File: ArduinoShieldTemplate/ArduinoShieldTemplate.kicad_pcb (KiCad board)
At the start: 2 copper layers, 68.6 x 53.3 mm, 31 parts, among them J1 M3, J2 M3, J3 M3, J4 Barrel_Jack_Switch, J5 UC_Screw_Terminal_01X02, J6 UC_Screw_Terminal_01X02, P1 Power, P2 Analog, P3 Digital, P4 Digital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

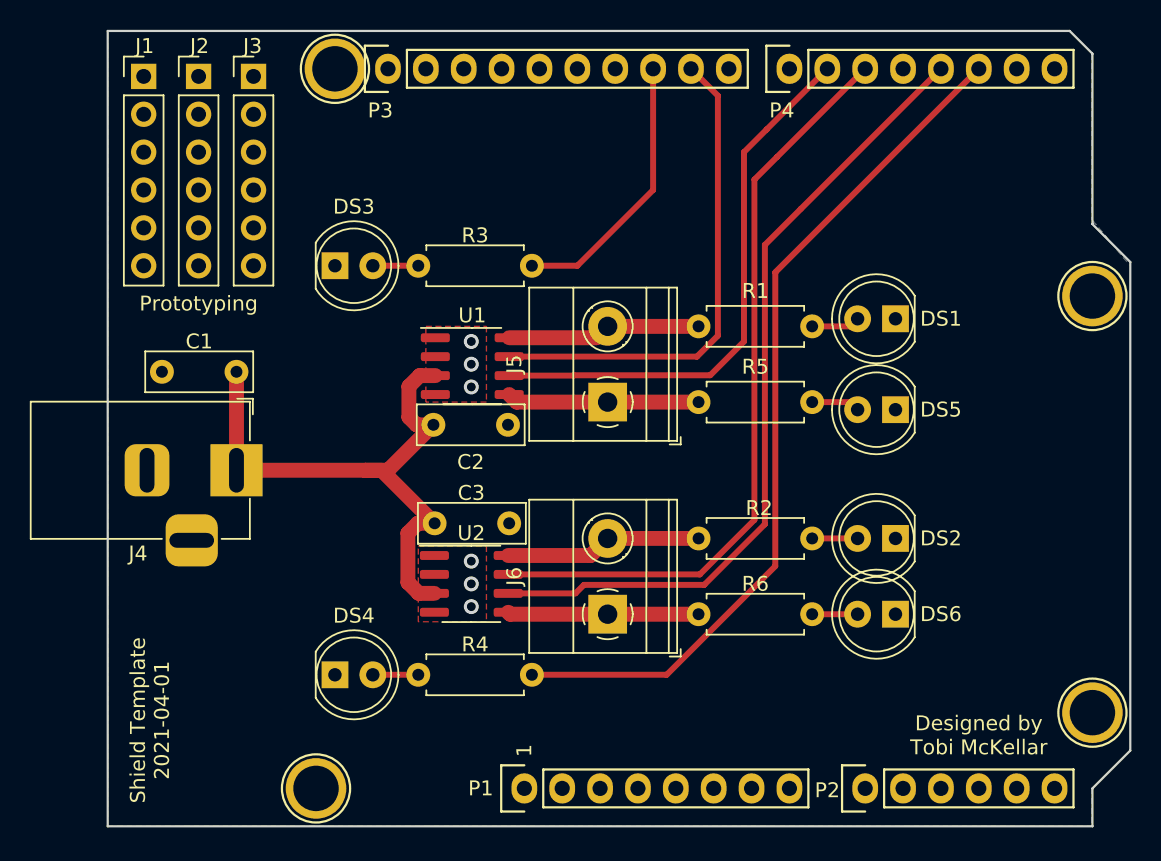
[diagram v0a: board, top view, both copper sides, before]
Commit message: cheeky rewiring for aesthetics
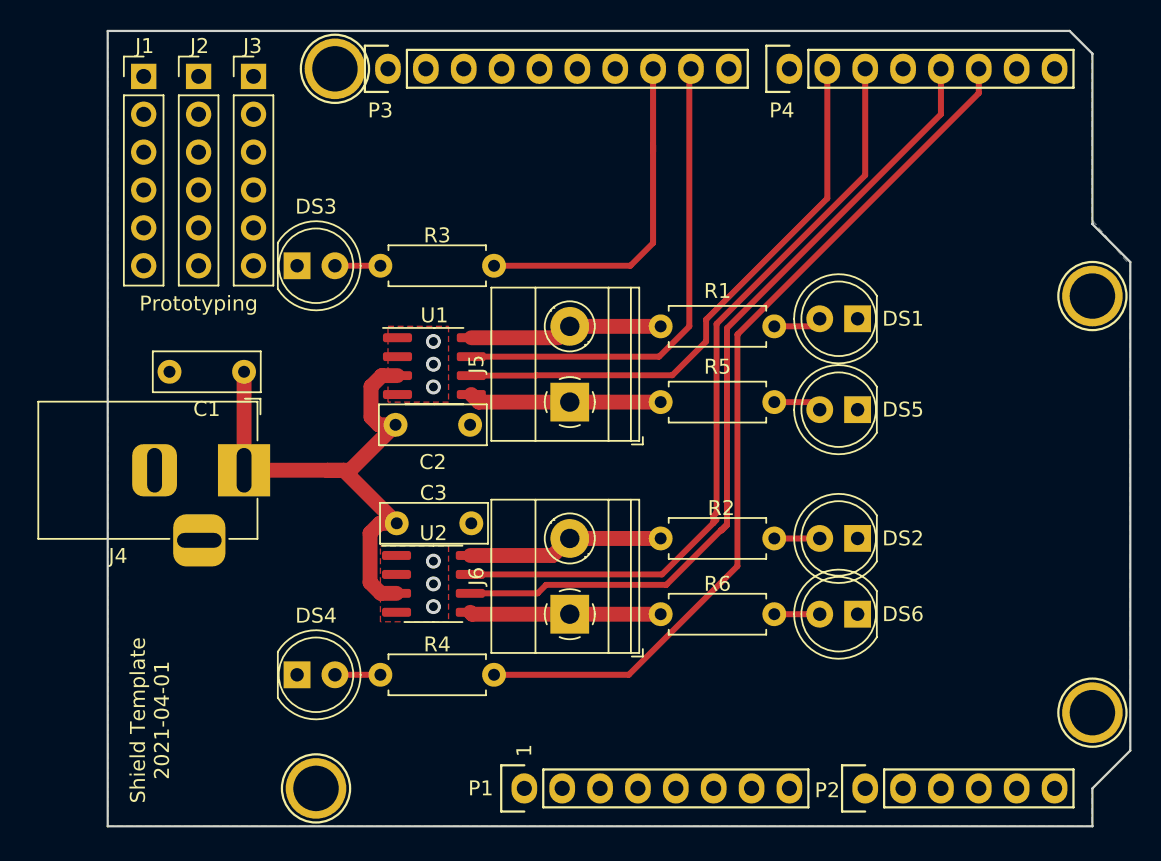
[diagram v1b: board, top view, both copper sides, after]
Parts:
- moved C2 2.54 mm to (135.3, 99.4)
- moved DS1 2.54 mm to (161.3, 92.3)
- moved DS2 2.54 mm to (161.3, 107.1)
- moved DS5 2.54 mm to (161.3, 98.4)
- moved DS6 2.54 mm to (161.3, 112.1)
- moved J5 2.54 mm to (142.0, 97.9)
- moved J6 2.54 mm to (142.0, 112.1)
- moved R1 2.54 mm to (148.1, 92.8)
- moved R2 2.54 mm to (148.1, 107.1)
- moved R5 2.54 mm to (148.1, 97.9)
- moved R6 2.54 mm to (148.1, 112.1)
- moved DS3 2.54 mm to (123.7, 88.8)
- moved DS4 2.54 mm to (123.7, 116.2)
- moved C3 2.54 mm to (135.4, 106.0)
- moved R3 2.54 mm to (136.9, 88.8)
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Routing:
- net /10(**SS): track 18.4 -> 23.5 mm
- net +5V: track 40.6 -> 37.6 mm
- net /3(**): track 54.6 -> 56.2 mm
- net /5(**): track 51.4 -> 52.7 mm
- net /2: track 58.3 -> 59.4 mm
- net /6(**): track 37.3 -> 38.3 mm
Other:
- board text removed: "Designed by Tobi McKellar"

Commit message: Fixing up the stuff design rules checker pointed out
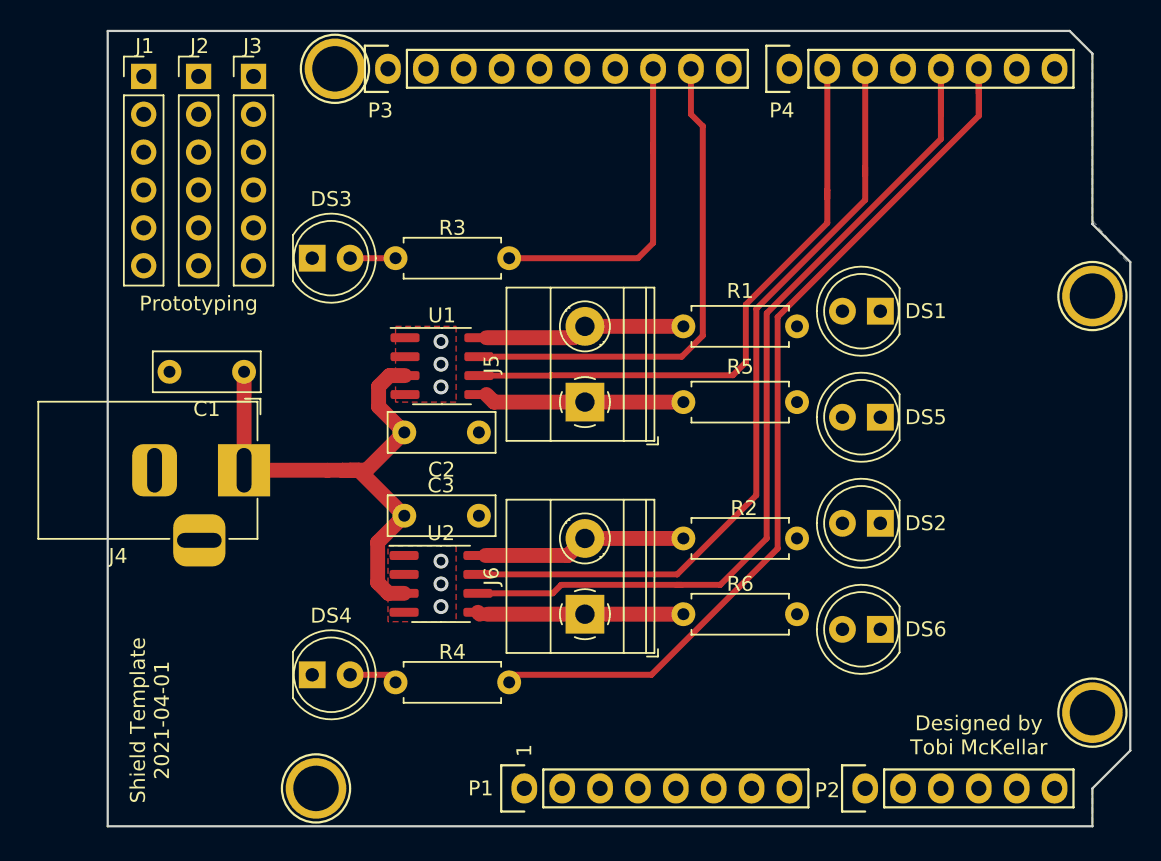
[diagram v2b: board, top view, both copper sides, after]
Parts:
- moved DS2 1.83 mm to (162.8, 106.0)
- moved DS6 1.83 mm to (162.8, 113.2)
- moved DS5 1.61 mm to (162.8, 98.9)
- moved DS1 1.61 mm to (162.8, 91.8)
- moved R1 1.52 mm to (149.6, 92.8)
- moved R2 1.52 mm to (149.6, 107.1)
- moved R5 1.52 mm to (149.6, 97.9)
- moved R6 1.52 mm to (149.6, 112.1)
- moved DS3 1.14 mm to (124.7, 88.3)
- moved R3 1.14 mm to (137.9, 88.3)
- moved R4 1.14 mm to (137.9, 116.7)
- moved J5 1.02 mm to (143.0, 97.9)
- moved J6 1.02 mm to (143.0, 112.1)
- moved DS4 1.02 mm to (124.7, 116.2)
- moved C2 0.78 mm to (135.9, 99.9)
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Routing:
- net /2: track 59.4 -> 64.0 mm
- net /3(**): track 56.2 -> 60.1 mm
- net Net-(DS1-Pad2): track 3.26 -> 0.00 mm
- net Net-(DS5-Pad2): track 3.26 -> 0.00 mm
- net Net-(DS6-Pad2): track 3.05 -> 0.00 mm
- net Net-(DS2-Pad2): track 3.05 -> 0.00 mm
- net /6(**): track 38.3 -> 40.3 mm
- net /10(**SS): track 23.5 -> 22.3 mm
- net /9(**): track 32.8 -> 33.5 mm
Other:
- board text added: "Designed by Tobi McKellar"
